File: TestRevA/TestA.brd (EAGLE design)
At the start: 45 x 50 mm, 51 parts, among them IC1 SI7021, IC2 ATMEGA328-PB, IC3 PE4259, IC4 NCS7SZ04, U1 V_REG_317SMD, U2 LSM9DS1, Y1 16MHz, Y2 16MHz

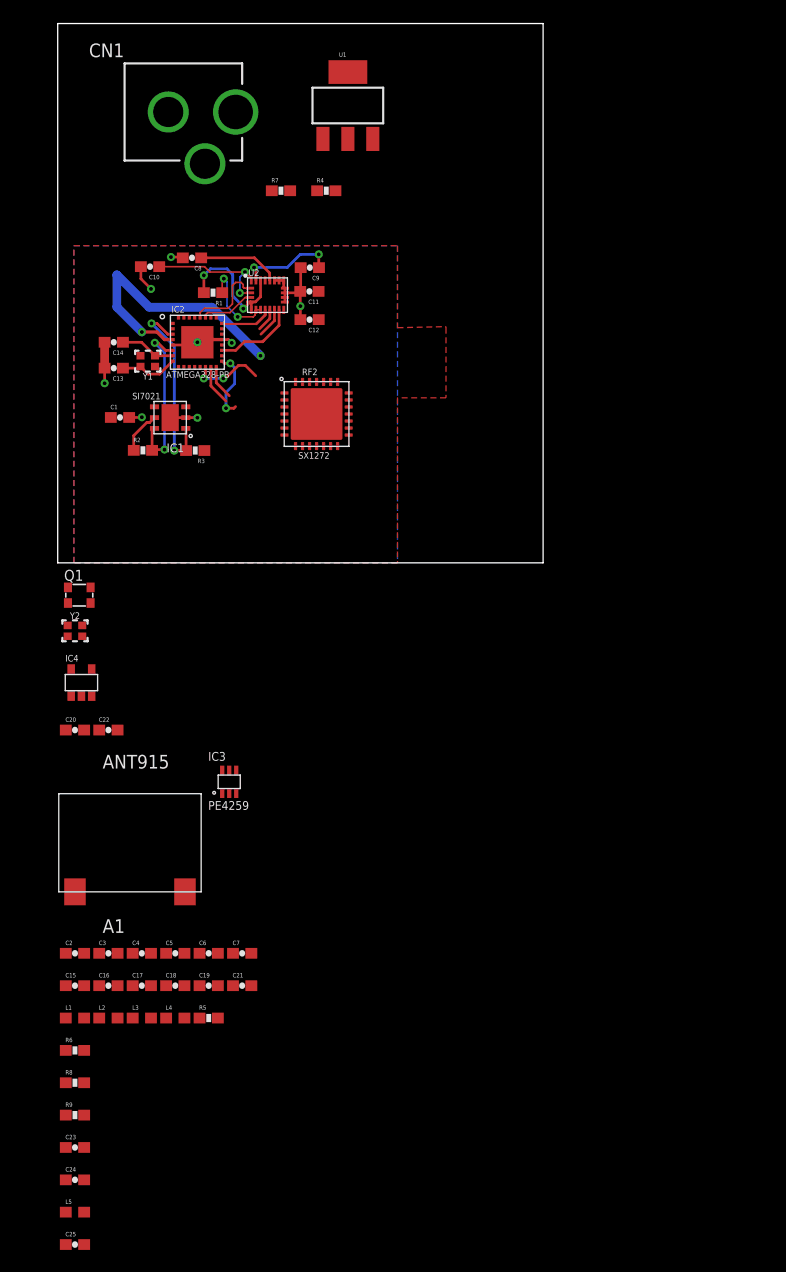
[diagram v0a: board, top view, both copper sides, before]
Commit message: Finished schematic
Got rid of UHF inverter, changed all components to 0402 from 0603, made DIO connections.
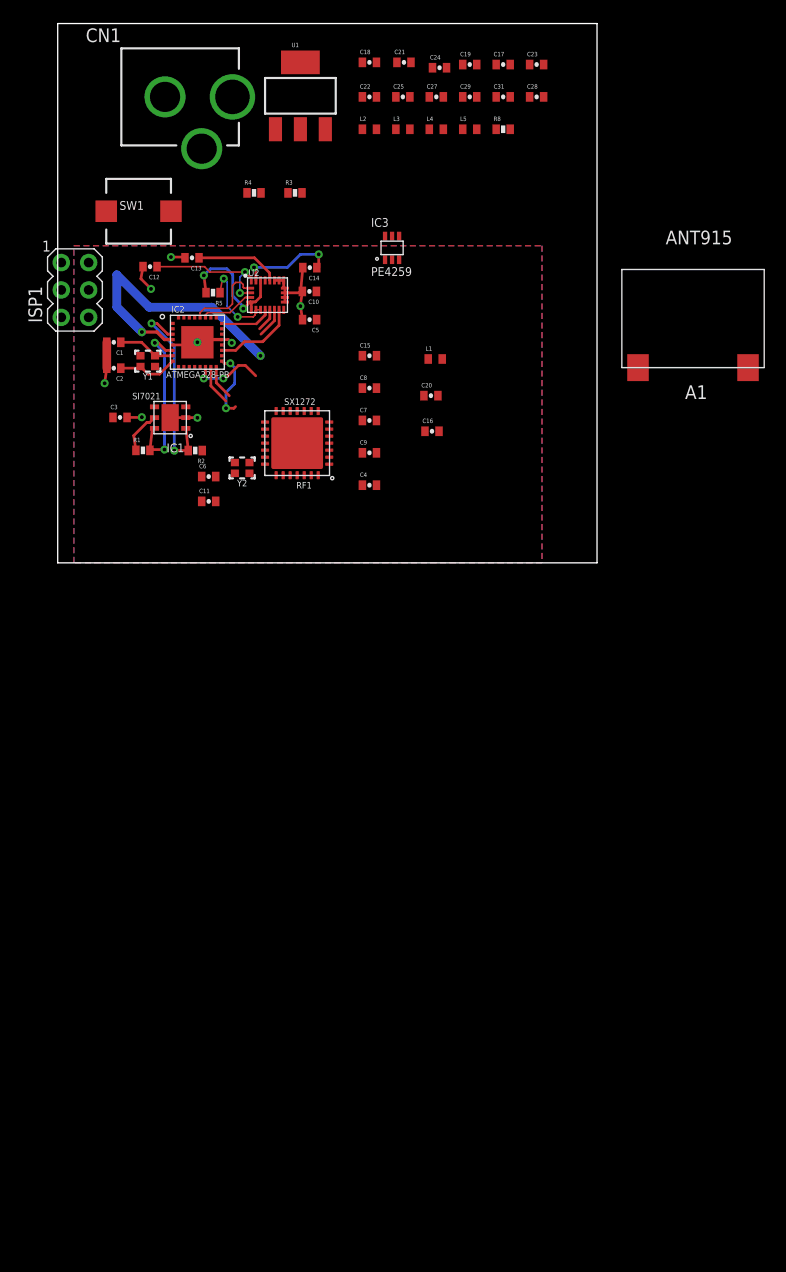
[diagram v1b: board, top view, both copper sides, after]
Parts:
- removed IC4: NCS7SZ04, Mini-Project:NC7SZ04
- removed Q1: (no value), crystal-geyer_V1_0:2.5X2.0_KXO-86-TCXO
- removed R6: nc, SparkFun:0603-RES
- removed R7: 360, SparkFun:0603-RES
- removed R9: 100, SparkFun:0603-RES
- removed RF2: SX1272, Mini-Project:SX1272
- added C27: 47pF, SparkFun:0402-CAP
- added C28: 1nF, SparkFun:0402-CAP
- added C29, C31: nc, SparkFun:0402-CAP
- added ISP1: AVRISP-6, adafruit:AVRISP
- added RF1: SX1272, Mini-Project:SX1272
- added SW1: (no value), adafruit:PUSHBUTTON_SMD_SJ
- C1: value 0.1 uF -> 26pF; device SparkFun:0603-CAP -> SparkFun:0402-CAP
- C10: value 0.1uF -> 10uF; device SparkFun:0603-CAP -> SparkFun:0402-CAP
- C11: value 10uF -> 10pF; device SparkFun:0603-CAP -> SparkFun:0402-CAP
- C12, C18: device SparkFun:0603-CAP -> SparkFun:0402-CAP
- C13: value 26pF -> 10nF; device SparkFun:0603-CAP -> SparkFun:0402-CAP
- C14: value 26pF -> 0.1uF; device SparkFun:0603-CAP -> SparkFun:0402-CAP
- C15: value 4.7pF -> 100nF; device SparkFun:0603-CAP -> SparkFun:0402-CAP
- C16: value 1.8pF -> 47pF; device SparkFun:0603-CAP -> SparkFun:0402-CAP
- C17: value 47pF -> 1.5pF; device SparkFun:0603-CAP -> SparkFun:0402-CAP
- C19: value nc -> 33pF; device SparkFun:0603-CAP -> SparkFun:0402-CAP
- C2: value nc -> 26pF; device SparkFun:0603-CAP -> SparkFun:0402-CAP
- C20: value 1nF -> 10nF; device SparkFun:0603-CAP -> SparkFun:0402-CAP
- C21: value 1nF -> 3.3pF; device SparkFun:0603-CAP -> SparkFun:0402-CAP
- C22: value 100nF -> 4.7pF; device SparkFun:0603-CAP -> SparkFun:0402-CAP
- C23: value 47pF -> 1.2pF; device SparkFun:0603-CAP -> SparkFun:0402-CAP
- C24: value 10nF -> 47pF; device SparkFun:0603-CAP -> SparkFun:0402-CAP
- C25: value 100nF -> 1.8pF; device SparkFun:0603-CAP -> SparkFun:0402-CAP
- C3: value 3.3pF -> 0.1 uF; device SparkFun:0603-CAP -> SparkFun:0402-CAP
- C4: value 47pF -> 1uF; device SparkFun:0603-CAP -> SparkFun:0402-CAP
- C5: value 33pF -> 0.1uF; device SparkFun:0603-CAP -> SparkFun:0402-CAP
- C6: value 1.5pF -> 10pF; device SparkFun:0603-CAP -> SparkFun:0402-CAP
- C7: value 1.2pF -> 100nF; device SparkFun:0603-CAP -> SparkFun:0402-CAP
- C8: value 10nF -> 100nF; device SparkFun:0603-CAP -> SparkFun:0402-CAP
- C9: value 0.1uF -> 100nF; device SparkFun:0603-CAP -> SparkFun:0402-CAP
- L1: value 10nF -> nc; device SparkFun:0603 -> SparkFun:C0402
- L2: value 10nH -> 10nF; device SparkFun:0603 -> SparkFun:C0402
- L3: value 6.2nH -> 10nH; device SparkFun:0603 -> SparkFun:C0402
- L4: value 0R -> 6.2nH; device SparkFun:0603 -> SparkFun:C0402
- L5: value nc -> 0R; device SparkFun:0603 -> SparkFun:C0402
- R1, R2: device SparkFun:0603-RES -> SparkFun:0402-RES
- R3: value 10K -> 220; device SparkFun:0603-RES -> SparkFun:0402-RES
- R4: value 220 -> 360; device SparkFun:0603-RES -> SparkFun:0402-RES
- R5: value 0 -> 10K; device SparkFun:0603-RES -> SparkFun:0402-RES
- R8: value nc -> 0; device SparkFun:0603-RES -> SparkFun:0402-RES
- Y2: value 16MHz -> 32Mhz
- moved C25 110.7 mm to (32.0, 43.2)
- moved C23 109.1 mm to (44.4, 46.2)
- moved C24 108.5 mm to (35.4, 45.9)
- moved L5 106.9 mm to (38.2, 40.2)
- moved R8 96.9 mm to (41.3, 40.2)
- moved C17 91.7 mm to (41.3, 46.2)
- moved C19 88.8 mm to (38.2, 46.2)
- moved C18 87.5 mm to (28.9, 46.4)
- moved C21 86.9 mm to (32.1, 46.4)
- moved L2 85.9 mm to (28.9, 40.2)
- moved L3 85.9 mm to (32.0, 40.2)
- moved L4 85.9 mm to (35.1, 40.2)
- moved A1 71.3 mm to (58.9, 18.1)
- moved L1 69.6 mm to (35.0, 18.9)
- moved R5 67.3 mm to (14.4, 25.1), turned to 180 degrees
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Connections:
- removed net GND/NC: Q1.1
- removed net N$19: C20.1, IC3.4, IC4.4, R6.2
- removed net N$20: C22.2, IC4.5
- removed net N$21: IC4.2, R6.1, R8.2, R9.2
- removed net RXTXEXT: R8.1
- removed net VDD: Q1.4
- new net DIO0: IC2.10, RF1.9
- new net DIO1: IC2.11, RF1.10
- new net DIO2: IC2.12, RF1.11
- new net DIO3: IC2.13, RF1.12
- new net N$23: IC2.24, ISP1.3
- new net N$24: C7.1, RF1.2
- new net N$25: C9.1, RF1.3
- new net N$26: IC2.23, ISP1.1
- new net N$27: IC2.22, ISP1.4
- new net XTA: C6.1, RF1.4, Y2.1
- new net XTB: C11.1, RF1.5, Y2.3
- net +3.3V: now also C10.1, C15.1, C28.1, C3.1, C5.1, C8.1, ISP1.2, R1.1, R5.2, RF1.1, RF1.15; no longer C1.1, C11.1, C12.1, C21.1, C25.1, R1.2, R3.1, RF2.15
- net 3.3V: now also C4.1, R3.2; no longer R4.2
- net GND: now also C17.2, C22.2, C28.2, C29.2, C31.2, C4.2, C5.2, C7.2, ISP1.6, R4.1, RF1.16, RF1.22, RF1.26, RF1.29, SW1.P$2; no longer C19.2, C22.1, C23.2, C24.2, IC4.3, Q1.2, R7.1, RF2.16, RF2.22, RF2.26, RF2.29
- net I1: now also IC2.32; no longer IC2.29
- net N$1: now also C24.1, R8.2; no longer C4.1, R5.2
- net N$10: now also C21.1, L2.2, R8.1; no longer C3.1, L1.2, R5.1
- net N$11: now also C17.1, C19.1, L1.1, RF1.24; no longer C5.1, C6.1, L5.1, RF2.24
- net N$12: now also C22.1, C23.1, L3.2, L4.1; no longer C15.1, C7.1, L2.2, L3.1
- net N$13: now also C19.2, L3.1; no longer C5.2, L2.1
- net N$14: now also C23.2, C25.1, IC3.1, L4.2; no longer C16.1, C7.2, IC3.3, L3.2
- net N$15: now also C31.1, L5.2; no longer C19.1, L4.2
- net N$16: now also C27.1; no longer C17.1
- net N$17: now also C14.1; no longer C9.1
- net N$18: now also C27.2, C29.1, L5.1; no longer C17.2, C18.1, L4.1
- net N$2: now also C16.1, C20.1, L1.2, RF1.28; no longer C23.1, C24.1, L5.2, RF2.28
- net N$22: now also IC2.29, ISP1.5, SW1.P$1; no longer RF2.6
- net N$4: now also C24.2, IC3.3; no longer C4.2, IC3.1
- net N$5: now also R5.1; no longer R1.1
- net N$6: now also R3.1, R4.2; no longer R4.1, R7.2
- net N$7: now also C18.1, L2.1, RF1.25; no longer C2.1, L1.1, RF2.25
- net N$8: now also C13.1; no longer C8.1
- net N$9: now also C12.1; no longer C10.1
- net RXTXX: now also IC3.4, RF1.23; no longer R9.1, RF2.23
- net SCK: now also RF1.17; no longer RF2.17
- net SCL: now also R1.2; no longer R2.2
- net SDA: now also R2.2; no longer R3.2
- net SI: now also RF1.19; no longer RF2.19
- net SO: now also RF1.18; no longer RF2.18
- net SS: now also RF1.20; no longer RF2.20
- net XTAL1: now also C1.1; no longer C14.1
- net XTAL2: now also C2.1; no longer C13.1
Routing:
- net GND: track 26.1 -> 26.9 mm
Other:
- board size 45 x 50 mm -> 50 x 50 mm

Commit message: Completed board design, DRC and finishing touches remaining
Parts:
- moved A1 44.7 mm to (17.1, 2.35)
- moved C31 40.1 mm to (12.7, 15.2)
- moved C28 38.7 mm to (19.3, 13.8), turned to 270 degrees
- moved C23 37.5 mm to (21.4, 16.6), turned to 180 degrees
- moved L5 36.7 mm to (10.1, 16.6), turned to 270 degrees
- moved ISP1 36.2 mm to (37.4, 30.4)
- moved C29 36.0 mm to (12.7, 17.9)
- moved C21 35.9 mm to (25.6, 11.1), turned to 180 degrees
- moved C27 34.9 mm to (12.7, 16.5), turned to 180 degrees
- moved C17 33.7 mm to (28.2, 15.2), turned to 180 degrees
- moved C24 33.7 mm to (25.6, 13.7), turned to 180 degrees
- moved C18 32.7 mm to (28.7, 13.7), turned to 180 degrees
- moved R8 31.9 mm to (25.6, 12.4), turned to 180 degrees
- moved C19 31.2 mm to (28.2, 16.6), turned to 180 degrees
- moved C25 29.0 mm to (24.5, 15.2)
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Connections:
- removed net SS: RF1.20
- new net DIO4: IC2.9, RF1.13
- new net DIO5: IC2.19, RF1.14
- net DIO0: now also IC2.13; no longer IC2.10
- net DIO1: now also IC2.12; no longer IC2.11
- net DIO2: now also IC2.11; no longer IC2.12
- net DIO3: now also IC2.10; no longer IC2.13
- net EN: now also RF1.20
- net I1: now also U2.9; no longer U2.11
- net I2: now also IC2.26; no longer IC2.19
- net I3: now also U2.10; no longer U2.9
- net I4: now also U2.11; no longer U2.10
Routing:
- net GND: track 26.9 -> 59.8 mm, vias 8 -> 23
- net DIO0: track 0.00 -> 21.2 mm
- net DIO1: track 0.00 -> 20.3 mm
- net RXTXX: track 0.00 -> 19.9 mm, vias 0 -> 2
- net DIO2: track 0.00 -> 19.6 mm
- net DIO3: track 0.00 -> 18.8 mm
- net DIO4: track 0.00 -> 18.1 mm
- net N$15: track 0.00 -> 15.0 mm
- net DIO5: track 0.00 -> 13.7 mm, vias 0 -> 2
- net N$26: track 0.00 -> 12.2 mm, vias 0 -> 2
- net N$27: track 0.00 -> 11.6 mm
- net N$22: track 0.00 -> 10.6 mm, vias 0 -> 2
- net N$2: track 0.00 -> 10.4 mm, vias 0 -> 2
- net N$4: track 0.00 -> 10.4 mm
- net N$3: track 0.00 -> 9.99 mm
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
